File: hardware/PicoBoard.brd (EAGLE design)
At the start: 110.5 x 59.1 mm, 44 parts, among them J1 AVR Prog., U1 FT232RLSSOP, U10 SLIDER, U2 ATMEGA328, U3 2.5mm, U4 2.5mm, U5 2.5mm, U6 2.5mm, U7 TEMT6000, U8 LMV358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

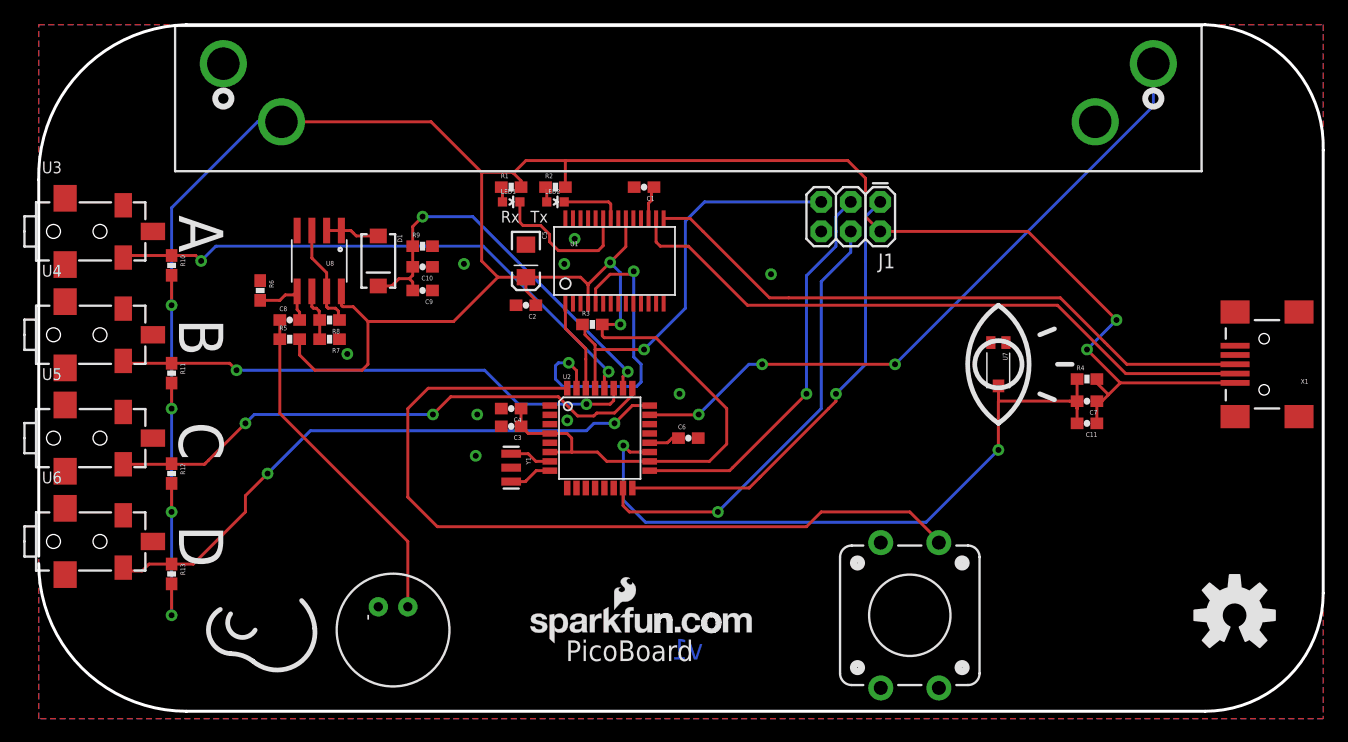
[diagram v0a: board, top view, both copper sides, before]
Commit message: Stereo Jack 1:1 updated
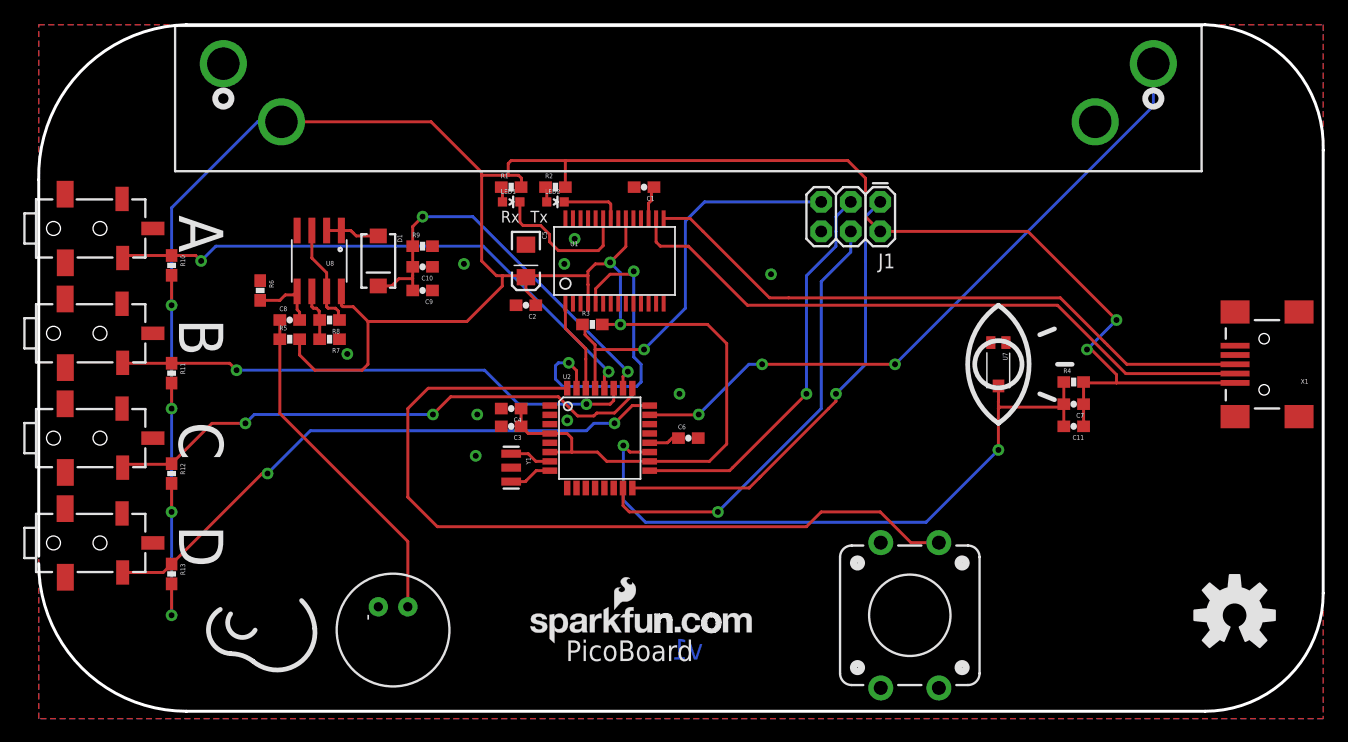
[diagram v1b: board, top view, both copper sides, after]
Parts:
- U3, U4, U5, U6: device SparkFun:STEREOJACK2.5MM_SMD -> Testing:STEREOJACKSMD1:1
- moved C7 1.17 mm to (89.0, 27.1)
- moved R4 1.17 mm to (89.0, 29.0)
- moved C11 1.17 mm to (89.0, 25.1)
- moved U3 0.25 mm to (1.27, 42.2)
- moved U6 0.13 mm to (1.27, 15.1)
- moved U4 0.13 mm to (1.27, 33.1)
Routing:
- net 5V: track 272.9 -> 277.3 mm
- net LIGHT: track 59.3 -> 57.9 mm
- net RD: track 52.2 -> 51.3 mm

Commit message: Trace clean up
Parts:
- moved LED2 0.77 mm to (43.7, 44.3)
- moved R2 0.51 mm to (43.9, 45.7)
- moved R1 0.25 mm to (40.4, 45.7)
- moved LED1 0.13 mm to (40.6, 44.3)
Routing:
- net RXLED: track 5.32 -> 5.96 mm
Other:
- board text added: "v11"
- board text removed: "v1"
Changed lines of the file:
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@@
 <layer number="27" name="tValues" color="7" fill="1" visible="no" active="yes"/>
 <layer number="28" name="bValues" color="7" fill="1" visible="no" active="yes"/>
-<layer number="29" name="tStop" color="7" fill="3" visible="yes" active="yes"/>
+<layer number="29" name="tStop" color="7" fill="3" visible="no" active="yes"/>
 <layer number="30" name="bStop" color="7" fill="6" visible="no" active="yes"/>
 <layer number="31" name="tCream" color="7" fill="4" visible="no" active="yes"/>
@@
 <layer number="106" name="bPlate" color="7" fill="1" visible="no" active="yes"/>
 <layer number="107" name="Crop" color="7" fill="1" visible="no" active="yes"/>
-<layer number="108" name="tplace-old" color="10" fill="1" visible="yes" active="yes"/>
-<layer number="109" name="ref-old" color="11" fill="1" visible="yes" active="yes"/>
+<layer number="108" name="tplace-old" color="10" fill="1" visible="no" active="yes"/>
+<layer number="109" name="ref-old" color="11" fill="1" visible="no" active="yes"/>
 <layer number="116" name="Patch_BOT" color="9" fill="4" visible="no" active="yes"/>
 <layer number="121" name="_tsilk" color="7" fill="1" visible="no" active="yes"/>
@@
 <text x="12.065" y="34.417" size="3.81" layer="21" font="vector" ratio="15" rot="SR270">B</text>
 <text x="12.065" y="43.307" size="3.81" layer="21" font="vector" ratio="15" rot="SR270">A</text>
-<text x="57.15" y="5.08" size="1.778" layer="16" font="vector" ratio="15" rot="MR0">v1</text>
-<text x="42.291" y="42.672" size="1.016" layer="21" font="vector" ratio="15">Tx</text>
-<text x="39.751" y="42.672" size="1.016" layer="21" font="vector" ratio="15">Rx</text>
+<text x="57.15" y="5.08" size="1.778" layer="16" font="vector" ratio="15" rot="MR0">v11</text>
+<text x="42.799" y="42.672" size="1.016" layer="21" font="vector" ratio="15">Tx</text>
+<text x="39.878" y="42.672" size="1.016" layer="21" font="vector" ratio="15">Rx</text>
 </plain>
 <attributes>
@@
 <element name="C1" library="SparkFun" package="0603-CAP" value="0.1uF" x="52.07" y="45.72" rot="R180"/>
 <element name="U1" library="SparkFun" package="SSOP28DB" value="FT232RLSSOP" x="49.53" y="39.37"/>
-<element name="R1" library="SparkFun" package="0603-RES" value="1K" x="40.64" y="45.72"/>
-<element name="R2" library="SparkFun" package="0603-RES" value="1K" x="44.45" y="45.72"/>
-<element name="LED1" library="SparkFun" package="LED-0603" value="Red" x="40.64" y="44.45" rot="R270"/>
-<element name="LED2" library="SparkFun" package="LED-0603" value="Green" x="44.45" y="44.45" rot="R270"/>
+<element name="R1" library="SparkFun" package="0603-RES" value="1K" x="40.386" y="45.72"/>
+<element name="R2" library="SparkFun" package="0603-RES" value="1K" x="43.942" y="45.72"/>
+<element name="LED1" library="SparkFun" package="LED-0603" value="Red" x="40.64" y="44.323" rot="R270"/>
+<element name="LED2" library="SparkFun" package="LED-0603" value="Green" x="43.688" y="44.323" rot="R270"/>
 <element name="U2" library="SparkFun" package="TQFP32-08" value="ATMEGA328" x="48.26" y="24.13"/>
 <element name="J1" library="SparkFun" package="2X3" value="AVR Prog." x="72.39" y="44.45" rot="R180"/>
@@
 <contactref element="U1" pad="23"/>
 <contactref element="LED1" pad="C"/>
-<wire x1="41.39" y1="42.684" x2="41.39" y2="44.45" width="0.254" layer="1"/>
+<wire x1="41.39" y1="42.684" x2="41.39" y2="44.323" width="0.254" layer="1"/>
 <wire x1="41.656" y1="42.418" x2="41.39" y2="42.684" width="0.254" layer="1"/>
 <wire x1="43.18" y1="42.418" x2="41.656" y2="42.418" width="0.254" layer="1"/>
@@
 <contactref element="U1" pad="22"/>
 <contactref element="LED2" pad="C"/>
-<wire x1="45.2" y1="44.45" x2="49.022" y2="44.45" width="0.254" layer="1"/>
-<wire x1="49.022" y1="44.45" x2="49.205" y2="44.267" width="0.254" layer="1"/>
-<wire x1="49.205" y1="44.267" x2="49.205" y2="43.026" width="0.254" layer="1"/>
+<wire x1="49.205" y1="43.026" x2="49.205" y2="44.14" width="0.254" layer="1"/>
+<wire x1="49.205" y1="44.14" x2="49.022" y2="44.323" width="0.254" layer="1"/>
+<wire x1="49.022" y1="44.323" x2="44.438" y2="44.323" width="0.254" layer="1"/>
 </signal>
 <signal name="N$1">
 <contactref element="R1" pad="1"/>
 <contactref element="LED1" pad="A"/>
-<wire x1="39.89" y1="44.45" x2="39.89" y2="45.72" width="0.254" layer="1"/>
-<wire x1="39.89" y1="45.72" x2="39.79" y2="45.72" width="0.254" layer="1"/>
+<wire x1="39.89" y1="44.323" x2="39.89" y2="45.72" width="0.254" layer="1"/>
+<wire x1="39.89" y1="45.72" x2="39.536" y2="45.72" width="0.254" layer="1"/>
 </signal>
 <signal name="N$2">
 <contactref element="R2" pad="1"/>
 <contactref element="LED2" pad="A"/>
-<wire x1="43.7" y1="44.45" x2="43.7" y2="45.72" width="0.254" layer="1"/>
-<wire x1="43.7" y1="45.72" x2="43.6" y2="45.72" width="0.254" layer="1"/>
+<wire x1="42.938" y1="44.323" x2="42.938" y2="45.72" width="0.254" layer="1"/>
+<wire x1="42.938" y1="45.72" x2="43.092" y2="45.72" width="0.254" layer="1"/>
 </signal>
 <signal name="TXO">
@@
 <wire x1="20.88" y1="51.34" x2="33.75" y2="51.34" width="0.254" layer="1"/>
 <wire x1="41.91" y1="37.97" x2="41.91" y2="38.1" width="0.254" layer="1"/>
-<wire x1="40.64" y1="48.006" x2="45.3" y2="48.006" width="0.254" layer="1"/>
-<wire x1="45.3" y1="48.006" x2="69.596" y2="48.006" width="0.254" layer="1"/>
+<wire x1="40.64" y1="48.006" x2="44.792" y2="48.006" width="0.254" layer="1"/>
+<wire x1="44.792" y1="48.006" x2="69.596" y2="48.006" width="0.254" layer="1"/>
 <wire x1="69.596" y1="48.006" x2="71.12" y2="46.482" width="0.254" layer="1"/>
 <wire x1="71.12" y1="46.482" x2="71.12" y2="43.18" width="0.254" layer="1"/>
@@
 <via x="90.17" y="31.75" extent="1-16" drill="0.508"/>
 <via x="92.71" y="34.29" extent="1-16" drill="0.508"/>
-<wire x1="45.3" y1="45.72" x2="45.3" y2="48.006" width="0.254" layer="1"/>
 <wire x1="42.76" y1="35.56" x2="42.76" y2="35.98" width="0.254" layer="1"/>
 <wire x1="42.76" y1="35.98" x2="41.91" y2="36.83" width="0.254" layer="1"/>
@@
 <wire x1="40.386" y1="47.752" x2="40.386" y2="46.736" width="0.254" layer="1"/>
 <wire x1="41.275" y1="46.736" x2="41.529" y2="46.482" width="0.254" layer="1"/>
-<wire x1="41.529" y1="46.482" x2="41.529" y2="45.759" width="0.254" layer="1"/>
-<wire x1="41.529" y1="45.759" x2="41.49" y2="45.72" width="0.254" layer="1"/>
+<wire x1="44.792" y1="45.72" x2="44.792" y2="48.006" width="0.254" layer="1"/>
+<wire x1="41.529" y1="46.482" x2="41.529" y2="46.013" width="0.254" layer="1"/>
+<wire x1="41.529" y1="46.013" x2="41.236" y2="45.72" width="0.254" layer="1"/>
 </signal>
 <signal name="N$5">
@@
 <wire x1="49.149" y1="27.051" x2="49.46" y2="27.362" width="0.254" layer="1"/>
 <wire x1="47.117" y1="27.051" x2="49.149" y2="27.051" width="0.254" layer="1"/>
-<wire x1="7.457" y1="30.77" x2="7.493" y2="30.734" width="0.254" layer="1"/>
-<wire x1="7.493" y1="30.734" x2="7.529" y2="30.77" width="0.254" layer="1"/>
 <via x="47.117" y="27.051" extent="1-16" drill="0.508"/>
 <via x="17.018" y="29.972" extent="1-16" drill="0.508"/>
@@
 <wire x1="11.43" y1="30.568" x2="7.2582" y2="30.568" width="0.254" layer="1"/>
 <wire x1="7.2582" y1="30.568" x2="7.2192" y2="30.607" width="0.254" layer="1"/>
-<wire x1="7.2582" y1="30.568" x2="7.457" y2="30.77" width="0" layer="19" extent="1-1"/>
 </signal>
 <signal name="RC">
@@
 <wire x1="18.542" y1="26.162" x2="33.909" y2="26.162" width="0.254" layer="16"/>
 <wire x1="17.78" y1="25.4" x2="18.542" y2="26.162" width="0.254" layer="16"/>
-<wire x1="7.584" y1="21.88" x2="7.62" y2="21.844" width="0.254" layer="1"/>
-<wire x1="7.62" y1="21.844" x2="7.656" y2="21.88" width="0.254" layer="1"/>
 <via x="33.909" y="26.162" extent="1-16" drill="0.508"/>
 <via x="17.78" y="25.4" extent="1-16" drill="0.508"/>
 <wire x1="11.43" y1="21.932" x2="14.898" y2="25.4" width="0.254" layer="1"/>
 <wire x1="14.898" y1="25.4" x2="17.78" y2="25.4" width="0.254" layer="1"/>
-<wire x1="11.43" y1="21.932" x2="11.378" y2="21.88" width="0.254" layer="1"/>
-<wire x1="11.378" y1="21.88" x2="7.5092" y2="21.88" width="0.254" layer="1"/>
-<wire x1="7.5092" y1="21.88" x2="7.2192" y2="21.59" width="0.254" layer="1"/>
-<wire x1="7.5092" y1="21.88" x2="7.584" y2="21.88" width="0" layer="19" extent="1-1"/>
+<wire x1="11.43" y1="21.932" x2="7.5612" y2="21.932" width="0.254" layer="1"/>
+<wire x1="7.5612" y1="21.932" x2="7.2192" y2="21.59" width="0.254" layer="1"/>
 </signal>
 <signal name="RD">
@@
 <wire x1="23.368" y1="24.765" x2="47.117" y2="24.765" width="0.254" layer="16"/>
 <wire x1="19.685" y1="21.082" x2="23.368" y2="24.765" width="0.254" layer="16"/>
-<wire x1="7.275" y1="12.99" x2="7.239" y2="12.954" width="0.254" layer="1"/>
 <via x="49.53" y="25.4" extent="1-16" drill="0.508"/>
 <via x="19.685" y="21.082" extent="1-16" drill="0.508"/>
@@
 <wire x1="11.43" y1="13.296" x2="10.707" y2="12.573" width="0.254" layer="1"/>
 <wire x1="10.707" y1="12.573" x2="7.2192" y2="12.573" width="0.254" layer="1"/>
-<wire x1="7.2192" y1="12.573" x2="7.239" y2="12.954" width="0" layer="19" extent="1-1"/>
 </signal>
 <signal name="SOUND">
